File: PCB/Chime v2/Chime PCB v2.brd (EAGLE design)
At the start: 62.2 x 77.6 mm, 34 parts, among them J1_I2C1 1725672, J2_I2C 1725672, J4_A1 282834-3, J5_A0 282834-3, U1 MS5803-02BA, X4 BQ24074

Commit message: Add files via upload
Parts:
- removed J1_I2C1: 1725672, 1725672:1725672
- removed J6_TSL2591: (no value), SparkFun-Connectors:1X06_LOCK
- removed J7_S3V, J8_S5V: (no value), SparkFun-Connectors:1X02
- added J1_SPI: 1725698, 1725698:1725698
- moved R3 0.36 mm to (20.1, 37.2)
- moved R8 0.25 mm to (21.8, 27.6)
- moved R4 0.18 mm to (16.3, 37.2)
- moved C5 0.13 mm to (19.7, 27.6)
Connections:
- removed net INT: J6_TSL2591.6
- removed net VIN: J6_TSL2591.1
- net 3VSWITCH: no longer J7_S3V.1
- net 5VSWITCH: no longer J8_S5V.1
- net A3: now also J1_SPI.3
- net GND: now also J1_SPI.2; no longer J1_I2C1.2, J6_TSL2591.3, J7_S3V.2, J8_S5V.2
- net MISO: now also J1_SPI.6
- net MOSI: now also J1_SPI.5
- net SCK: now also J1_SPI.4
- net SCL: no longer J1_I2C1.3, J6_TSL2591.4
- net SDA: no longer J1_I2C1.4, J6_TSL2591.5
- net VCC: now also J1_SPI.1; no longer J1_I2C1.1, J6_TSL2591.2
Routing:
- net SCK: track 0.00 -> 65.5 mm
- net A3: track 0.00 -> 63.8 mm
- net MOSI: track 0.00 -> 63.7 mm
- net MISO: track 0.00 -> 62.8 mm
- net 3VSWITCH: track 41.3 -> 0.00 mm, vias 1 -> 0
- net 5VSWITCH: track 35.6 -> 0.00 mm, vias 1 -> 0
- net SCL: track 78.0 -> 49.8 mm
- net SDA: track 84.4 -> 66.4 mm
- net VCC: track 179.0 -> 161.6 mm, vias 2 -> 0
- net A1: track 57.8 -> 60.3 mm
- net VLIPO: track 15.8 -> 16.4 mm
- added copper zone on layer 16, net VCC
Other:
- board size 62.2 x 77.6 mm -> 64.8 x 78.8 mm
- board text added: "A3"
- board text added: "MISO"
- board text added: "MOSI"
- board text added: "SCK"
- board text removed: "3V_SWITCH"
- board text removed: "5V_SWITCH"

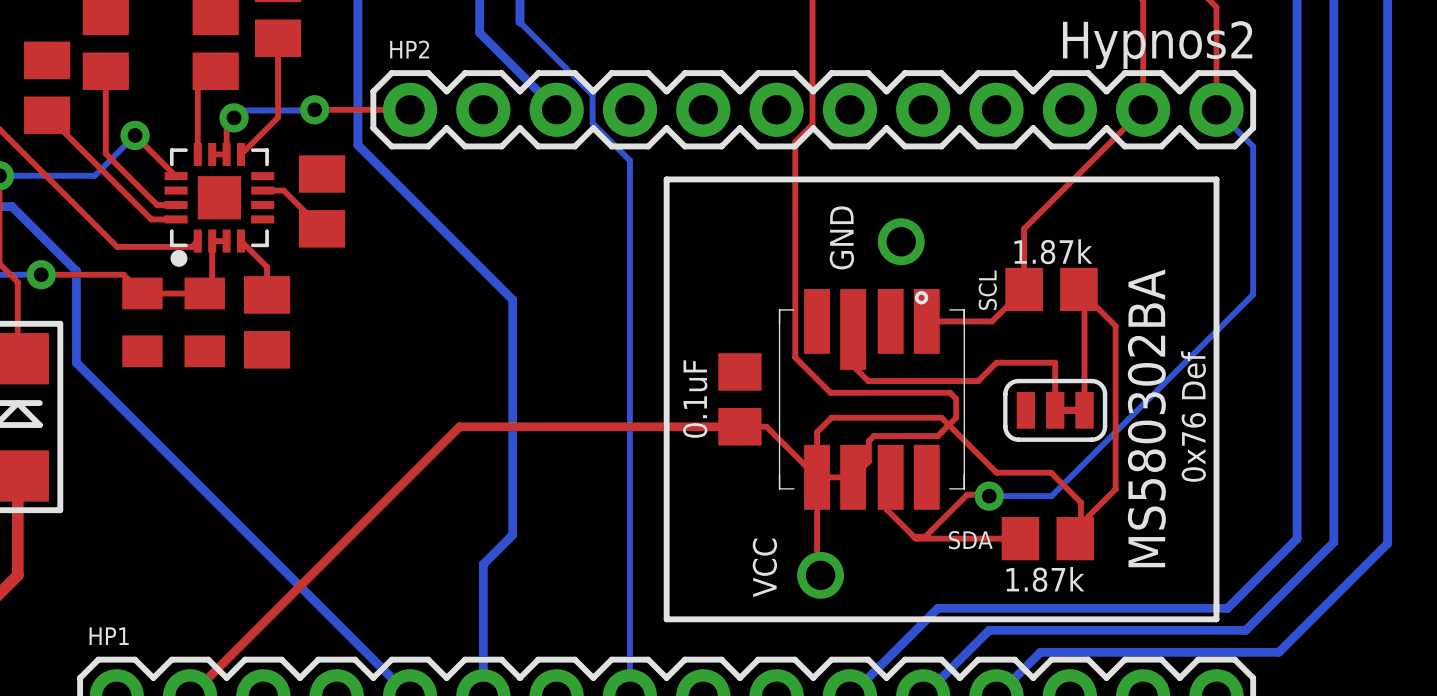
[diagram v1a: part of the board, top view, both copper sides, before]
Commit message: Air Wiring Issue resolved
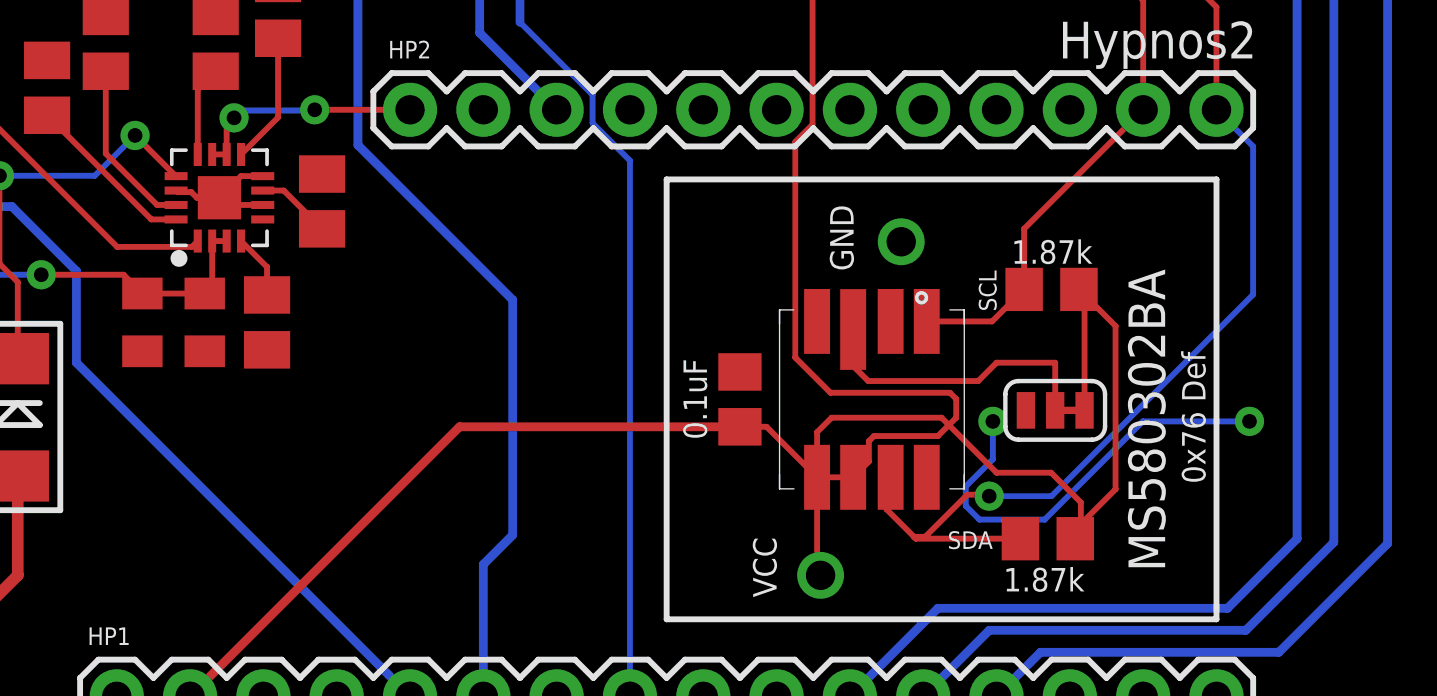
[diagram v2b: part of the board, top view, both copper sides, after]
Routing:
- net GND: track 0.00 -> 19.8 mm, vias 0 -> 2
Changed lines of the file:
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@@
 <drawing>
 <settings>
-<setting alwaysvectorfont="yes"/>
+<setting alwaysvectorfont="no"/>
 <setting verticaltext="up"/>
 </settings>
@@
 <vertex x="-1.27" y="-1.27"/>
 </polygon>
-<wire x1="33.02" y1="66.04" x2="48.26" y2="66.04" width="0" layer="19" extent="1-1"/>
-<wire x1="31.75" y1="58.42" x2="33.02" y2="66.04" width="0" layer="19" extent="1-1"/>
-<wire x1="17.78" y1="66.04" x2="33.02" y2="66.04" width="0" layer="19" extent="1-1"/>
-<wire x1="5.08" y1="66.04" x2="17.78" y2="66.04" width="0" layer="19" extent="1-1"/>
-<wire x1="20.066" y1="38.161" x2="31.75" y2="58.42" width="0" layer="19" extent="1-1"/>
-<wire x1="16.256" y1="38.161" x2="20.066" y2="38.161" width="0" layer="19" extent="1-1"/>
-<wire x1="14.224" y1="36.637" x2="16.256" y2="38.161" width="0" layer="19" extent="1-1"/>
-<wire x1="21.693" y1="32.627" x2="20.066" y2="38.161" width="0" layer="19" extent="1-1"/>
-<wire x1="21.693" y1="31.627" x2="21.693" y2="32.627" width="0" layer="19" extent="1-1"/>
-<wire x1="20.193" y1="31.877" x2="21.693" y2="31.627" width="0" layer="19" extent="1-1"/>
-<wire x1="18.693" y1="32.127" x2="20.193" y2="31.877" width="0" layer="19" extent="1-1"/>
-<wire x1="21.844" y1="26.609" x2="21.693" y2="31.627" width="0" layer="19" extent="1-1"/>
-<wire x1="19.685" y1="26.559" x2="21.844" y2="26.609" width="0" layer="19" extent="1-1"/>
-<wire x1="17.526" y1="26.559" x2="19.685" y2="26.559" width="0" layer="19" extent="1-1"/>
-<wire x1="8.526" y1="23.003" x2="17.526" y2="26.559" width="0" layer="19" extent="1-1"/>
-<wire x1="2.921" y1="34.163" x2="14.224" y2="36.637" width="0" layer="19" extent="1-1"/>
-<wire x1="24.257" y1="14.605" x2="21.844" y2="26.609" width="0" layer="19" extent="1-1"/>
-<wire x1="17.78" y1="10.16" x2="24.257" y2="14.605" width="0" layer="19" extent="1-1"/>
-<wire x1="38.227" y1="25.842" x2="21.844" y2="26.609" width="0" layer="19" extent="1-1"/>
-<wire x1="43.449" y1="27.592" x2="38.227" y2="25.842" width="0" layer="19" extent="1-1"/>
-<wire x1="43.815" y1="30.353" x2="43.449" y2="27.592" width="0" layer="19" extent="1-1"/>
-<wire x1="48.133" y1="24.511" x2="43.449" y2="27.592" width="0" layer="19" extent="1-1"/>
+<wire x1="18.693" y1="32.127" x2="18.7482" y2="32.0718" width="0.2032" layer="1"/>
+<wire x1="18.7482" y1="32.0718" x2="19.21925" y2="32.0718" width="0.2032" layer="1"/>
+<wire x1="19.41405" y1="31.877" x2="20.193" y2="31.877" width="0.2032" layer="1"/>
+<wire x1="19.21925" y1="32.0718" x2="19.41405" y2="31.877" width="0.2032" layer="1"/>
+<wire x1="20.193" y1="31.877" x2="20.443" y2="31.627" width="0.2032" layer="1"/>
+<wire x1="20.443" y1="31.627" x2="21.693" y2="31.627" width="0.2032" layer="1"/>
+<wire x1="20.193" y1="31.877" x2="20.943" y2="32.627" width="0.2032" layer="1"/>
+<wire x1="20.943" y1="32.627" x2="21.693" y2="32.627" width="0.2032" layer="1"/>
+<via x="46.99" y="24.13" extent="1-16" drill="0.508"/>
+<via x="55.88" y="24.13" extent="1-16" drill="0.508"/>
+<wire x1="46.0502" y1="21.875875" x2="46.0502" y2="21.202525" width="0.2032" layer="16"/>
+<wire x1="46.0502" y1="21.202525" x2="46.526325" y2="20.7264" width="0.2032" layer="16"/>
+<wire x1="52.1875375" y1="24.13" x2="55.88" y2="24.13" width="0.2032" layer="16"/>
+<wire x1="46.526325" y1="20.7264" x2="48.7839375" y2="20.7264" width="0.2032" layer="16"/>
+<wire x1="48.7839375" y1="20.7264" x2="52.1875375" y2="24.13" width="0.2032" layer="16"/>
+<wire x1="46.99" y1="24.13" x2="46.99" y2="22.815675" width="0.2032" layer="16"/>
+<wire x1="46.99" y1="22.815675" x2="46.0502" y2="21.875875" width="0.2032" layer="16"/>
 </signal>
 <signal name="VCC">
